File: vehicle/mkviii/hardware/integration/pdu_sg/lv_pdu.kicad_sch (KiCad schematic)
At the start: 0 parts

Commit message: ampseals
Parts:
- added D2: D_Red_LED, OEM:D_0805_2012Metric, symbol OEM:D_LED_Red_0805
- added D3: D_Amber_LED, Diode_SMD:D_0805_2012Metric, symbol OEM_mkvii:D_LED_Amber_0805
- added J10, J11, J12, J9: Conn_01x03, Connector_PinHeader_2.54mm:PinHeader_1x03_P2.54mm_Vertical, symbol Connector_Generic:Conn_01x03
- added J13, J14: J_Ampseal_23_RA, OEM:J_Ampseal_23_RA, symbol OEM:J_Ampseal_23_RA
- added J2, J3: J_Ampseal_14_RA, OEM:J_Ampseal_14_RA, symbol OEM:J_Ampseal_14_RA
- added J4, J5, J6, J7, J8: J_Ampseal_08_RA, OEM:J_Ampseal_8_RA, symbol OEM:J_Ampseal_08_RA
- added R2: R_200_0.1W, OEM:R_0603_1608Metric, symbol OEM:R_200_0.1W_0603
- added R3: R_1k_0.1W, OEM:R_0603_1608Metric, symbol OEM:R_1k_0.1W_0603
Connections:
- new net: D3.2 (A), R3.2
- new net: D2.2 (A), R2.2
- new net +5V: J13.8, J14.8
- new net 12V_COOLING_OUT: J3.3, J3.4
- new net 12V_IN: J5.4, J5.6
- new net 12V_LV: J7.4, J7.6
- new net 12V_MC: J2.7
- new net 12V_PDU: J13.12, J13.16, J14.12, J14.16, J4.4, J8.5, J8.7
- new net 12V_SHDN: J11.1 (Pin_1), J8.1
- new net 12V_SS: J6.3
- new net CAN_1+: J4.2, J5.2
- new net CAN_1-: J4.3, J5.3
- new net CAN_2+: J14.18, J4.7
- new net CAN_2-: J14.19, J4.6
- new net CAN_3+: J13.18, J14.20
- new net CAN_3-: J13.19, J14.21
- new net CAN_4+: J13.20, J2.8
- new net CAN_4-: J13.21, J2.9
- new net CAN_5+: J2.4
- new net CAN_5-: J2.5
- new net CAN_6+: J7.2
- new net CAN_6-: J7.3
- new net EXCITATION_L+: J13.3
- new net EXCITATION_L-: J13.4
- new net EXCITATION_R+: J14.3
- new net EXCITATION_R-: J14.4
- new net E_STOP_COM: J11.2 (Pin_2), J12.1 (Pin_1), J8.2
- new net E_STOP_R_OUT: J10.1 (Pin_1), J12.2 (Pin_2), J2.11, J8.3
- new net GND: D2.1 (K), D3.1 (K), J13.13, J13.17, J13.22, J13.23, J13.9, J14.13, J14.17, J14.22, J14.23, J14.9, J2.3, J3.2, J3.5, J3.8, J4.1, J4.5, J5.1, J5.5, J6.1, J6.2, J7.1, J7.5
- new net HVIL_OUT: J10.2 (Pin_2), J2.10
- new net INVERTER_FAULT: J2.13, R2.1
- new net INVERTER_GND: J2.6, J9.2 (Pin_2)
- new net INVERTER_PROGRAM: J2.12, J9.3 (Pin_3)
- new net INVERTER_RXD: J2.1
- new net INVERTER_START_OK: R3.1
- new net INVERTER_START_OUT: J2.14
- new net INVERTER_TXD: J2.2
- new net SHDN_IN: J7.8
- new net SIGNAL_L+: J13.6
- new net SIGNAL_L-: J13.5
- new net SIGNAL_R-: J14.5
- new net SIGNAL_R_+: J14.6
- new net SIG_FAN: J3.9
- new net SIG_PUMP: J3.7
- new net SIG_TEMP: J3.6
- new net SUS_TRAVEL_L_SIG: J13.10
- new net SUS_TRAVEL_R_SIG: J14.10
- new net TSMS_IN: J5.7, J6.7
- new net TSMS_OUT: J5.8, J6.8
- new net TS_STAT_G_12V: J8.6
- new net TS_STAT_R_12V: J8.8
- new net WHEEL_SPEED_L_SIG: J13.14
- new net WHEEL_SPEED_R_SIG: J14.14
- no-connect marks 0 -> 26
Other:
- note added: "CAN"
- note removed: "Controller Area Network (CAN)"

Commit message: ampseal labels + reorganizing
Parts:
- renumbered J4 to AUX_DEVICE_GPS1, J3 to COOLING1, J7 to LV_MOBO, J2 to MC1, J5 to MSB, J8 to ROLLHOOP, J13 to SENSE_L_WHEEL_AMPSEAL, J14 to SENSE_R_WHEEL_AMPSEAL, J6 to SERVICE_SECTION
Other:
- moved on the sheet: AUX_DEVICE_GPS1, D2, D3, J10, J11, J12, J9, LV_MOBO, MSB, R2, R3, ROLLHOOP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

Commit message: reorganizing
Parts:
- added TP1, TP2: TP_SMD, OEM:TP_Hook_SMD, symbol OEM_mkvii:TP_Hook_SMD
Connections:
- net 12V_IN renamed +12V
- new net CAN_IN+: TP1.1
- new net CAN_IN-: TP2.1
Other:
- added sheet low voltage distribution (lv_db.kicad_sch)
- added sheet sensor boards (sensing_connections.kicad_sch)
- sheet microcontroller ports: added CAN_OUT+, CAN_OUT-, COOLING_EN, FAN_PWM, PUMP_PWM, SS_ESTOP_L, SS_ESTOP_R, SS_GLVMS, SS_MC, TS_STATUS_G, TS_STATUS_R; removed none
- note added: "Sensors"
- note removed: "To Sensors"

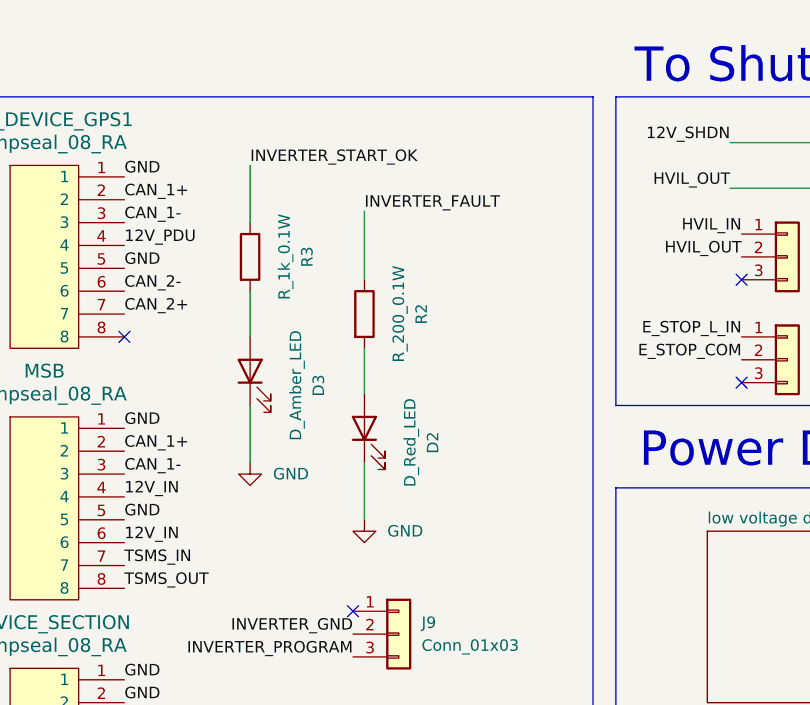
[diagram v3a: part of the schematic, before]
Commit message: fix inverter_fault inverter_start_ok led
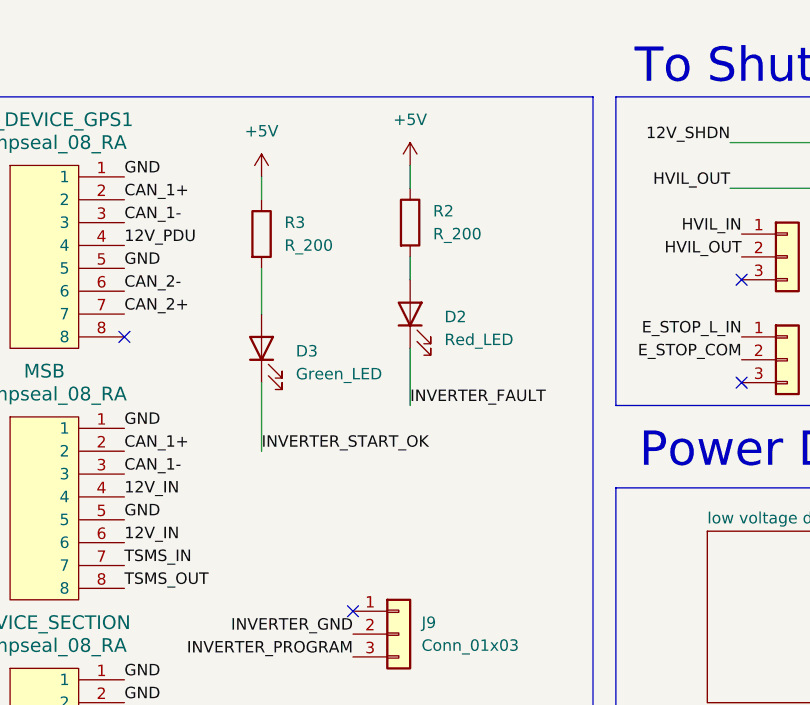
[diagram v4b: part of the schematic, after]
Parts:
- removed D3: D_Amber_LED, Diode_SMD:D_0805_2012Metric, symbol OEM_mkvii:D_LED_Amber_0805
- removed R3: R_1k_0.1W, OEM:R_0603_1608Metric, symbol OEM:R_1k_0.1W_0603
- added D3: Green_LED, OEM:D_0805_2012Metric, symbol OEM:D_LED_Green_0805
- added R3: R_200, OEM:R_0603_1608Metric, symbol OEM:R_200_0.1W_0603
- D2: value D_Red_LED -> Red_LED
- R2: value R_200_0.1W -> R_200
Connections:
- net +5V: now also R2.1, R3.1
- net GND: no longer D2.1 (K)
- net INVERTER_FAULT: now also D2.1 (K); no longer R2.1
- net INVERTER_START_OK: now also D3.1 (K)
- new net: D3.2 (A), R3.2

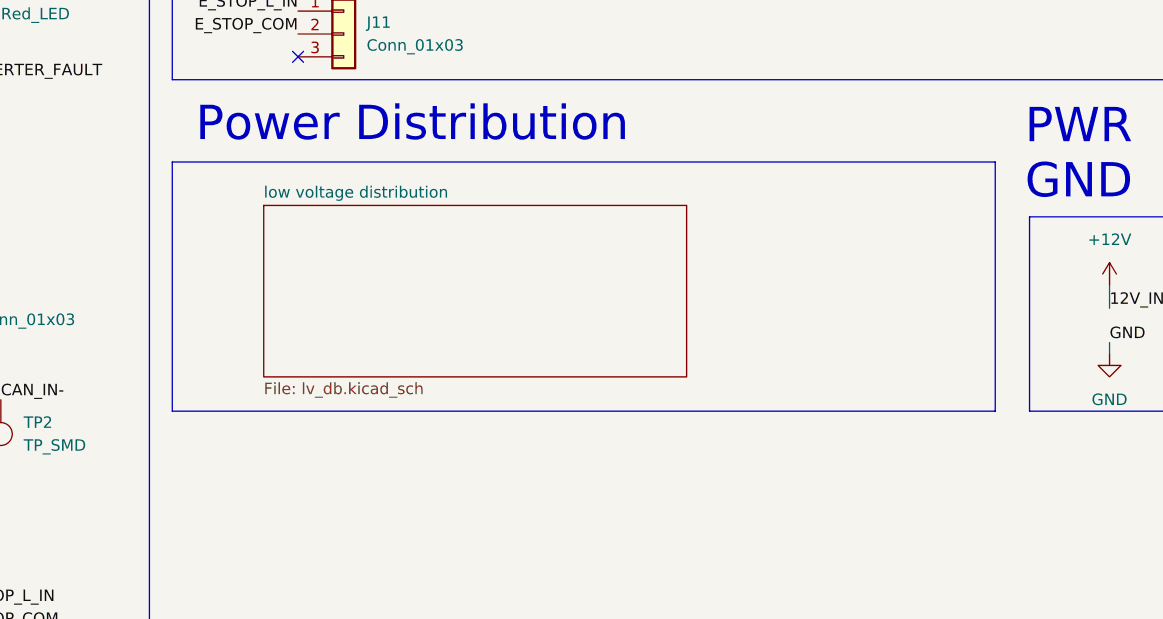
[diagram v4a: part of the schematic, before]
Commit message: lv power distribution + rs232
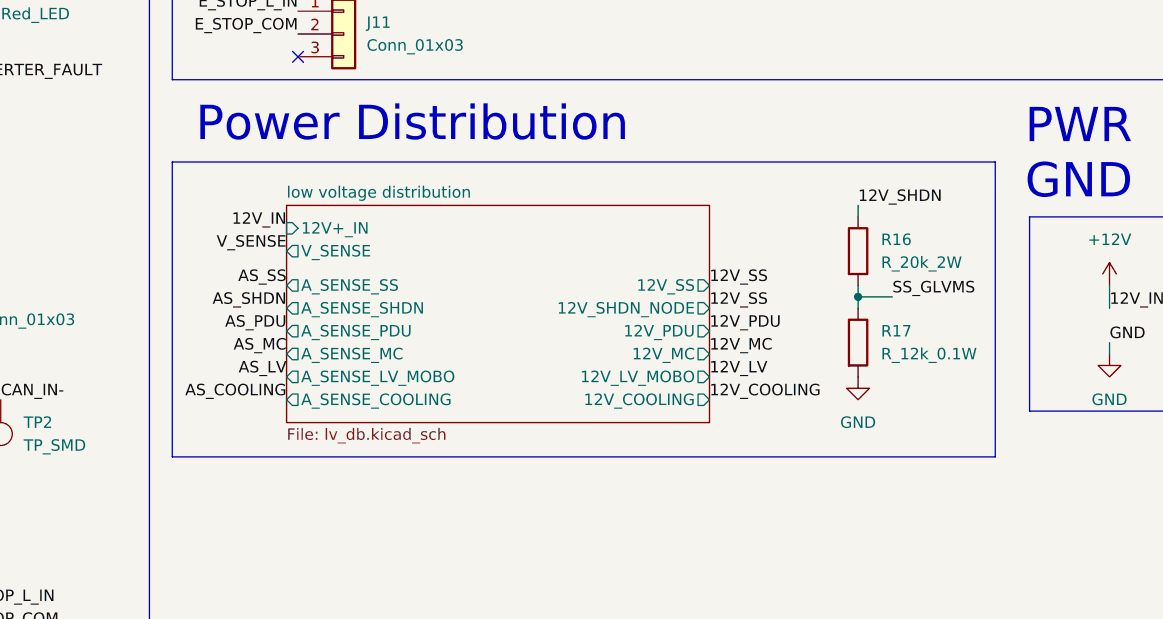
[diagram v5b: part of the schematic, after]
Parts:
- added R16: R_20k_2W, OEM:R_2512_6332Metric, symbol OEM:R_20k_2W_2512
- added R17: R_12k_0.1W, OEM:R_0603_1608Metric, symbol OEM:R_12k_0.1W_0603
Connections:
- net 12V_SHDN: now also R16.1
- net GND: now also R17.2
- net SS_GLVMS: now also R16.2, R17.1
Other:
- sheet low voltage distribution ports: added 12V+_IN, 12V_COOLING, 12V_LV_MOBO, 12V_MC, 12V_PDU, 12V_SHDN_NODE, 12V_SS, A_SENSE_COOLING, A_SENSE_LV_MOBO, A_SENSE_MC, A_SENSE_PDU, A_SENSE_SHDN, A_SENSE_SS, V_SENSE; removed none

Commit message: adc
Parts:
- added J2: J_DSub-9, OEM:TE_5745781-4, symbol OEM:J_DSub-9
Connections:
- net INVERTER_GND: now also J2.5
- net INVERTER_RXD: now also J2.2
- net INVERTER_TXD: now also J2.3
- no-connect marks 26 -> 32
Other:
- sheet microcontroller ports: added A_COOLING, A_LV_MOBO, A_MC, A_PDU, A_SHDN, A_SS, SIG_TEMP, V_SENSE; removed none
- note added: "RS232"

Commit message: implement can control
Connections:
- net SIGNAL_R_+ renamed SIGNAL_R+
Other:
- added sheet CAN control (CAN_control.kicad_sch)
- sheet sensor boards ports: added 5V, 5V_L, 5V_R, CAN+, CAN-, GND, GND_L, GND_R, LIN_POT_L, LIN_POT_R, SIG_L+, SIG_L-, SIG_R+, SIG_R-, WHEEL_SPEED_L_SENSE, WHEEL_SPEED_R_SENSE; removed none
- note added: "GPS Short"
- note added: "LV MOBO"
- note added: "MC SHORT"
- note added: "MSB"
- note added: "Suspension Strain"
- note added: "Suspension Travel"
- note added: "WHEEL_L SHORT"
- note added: "WHEEL_R SHORT"
- note added: "Wheel Speed"
- moved on the sheet: J2

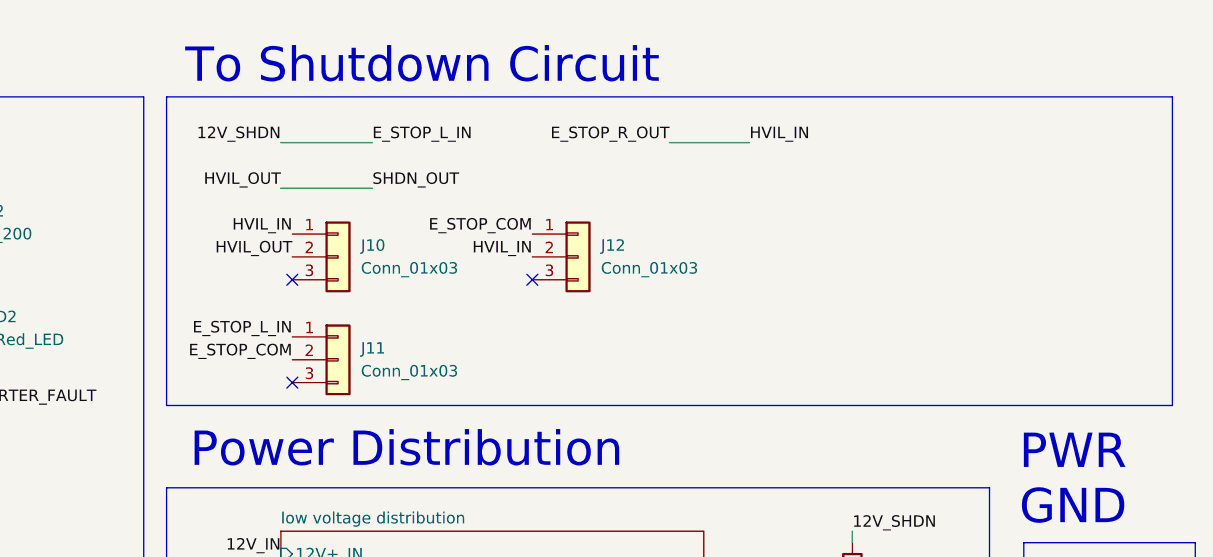
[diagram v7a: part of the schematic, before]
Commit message: shutdown sense input conversion
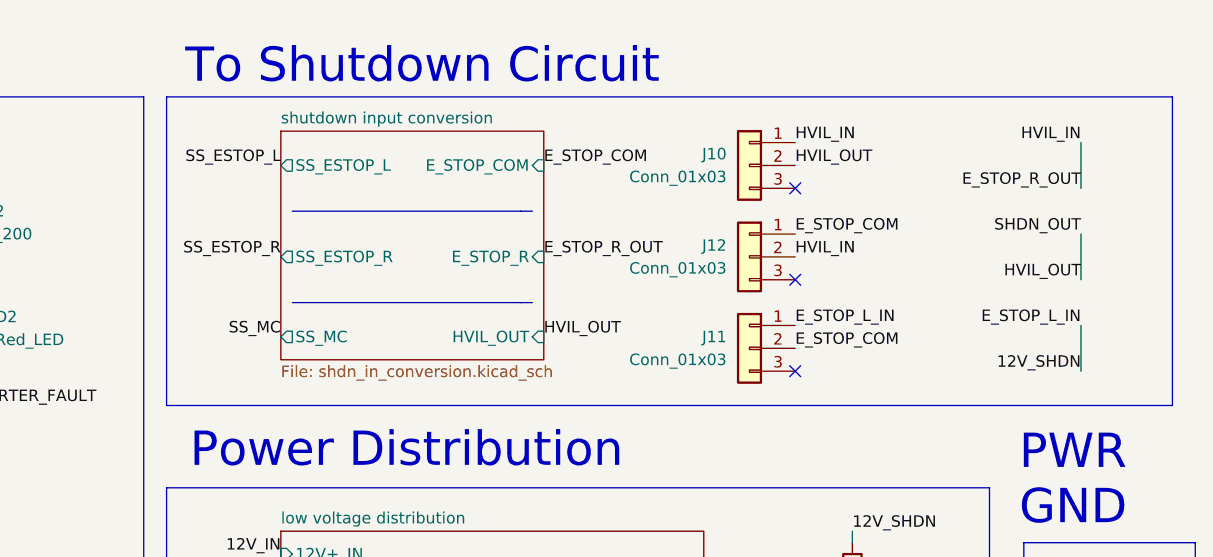
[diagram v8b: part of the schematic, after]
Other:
- added sheet shutdown input conversion (shdn_in_conversion.kicad_sch)
- moved on the sheet: J10, J11, J12
